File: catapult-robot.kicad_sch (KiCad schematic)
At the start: 15 parts

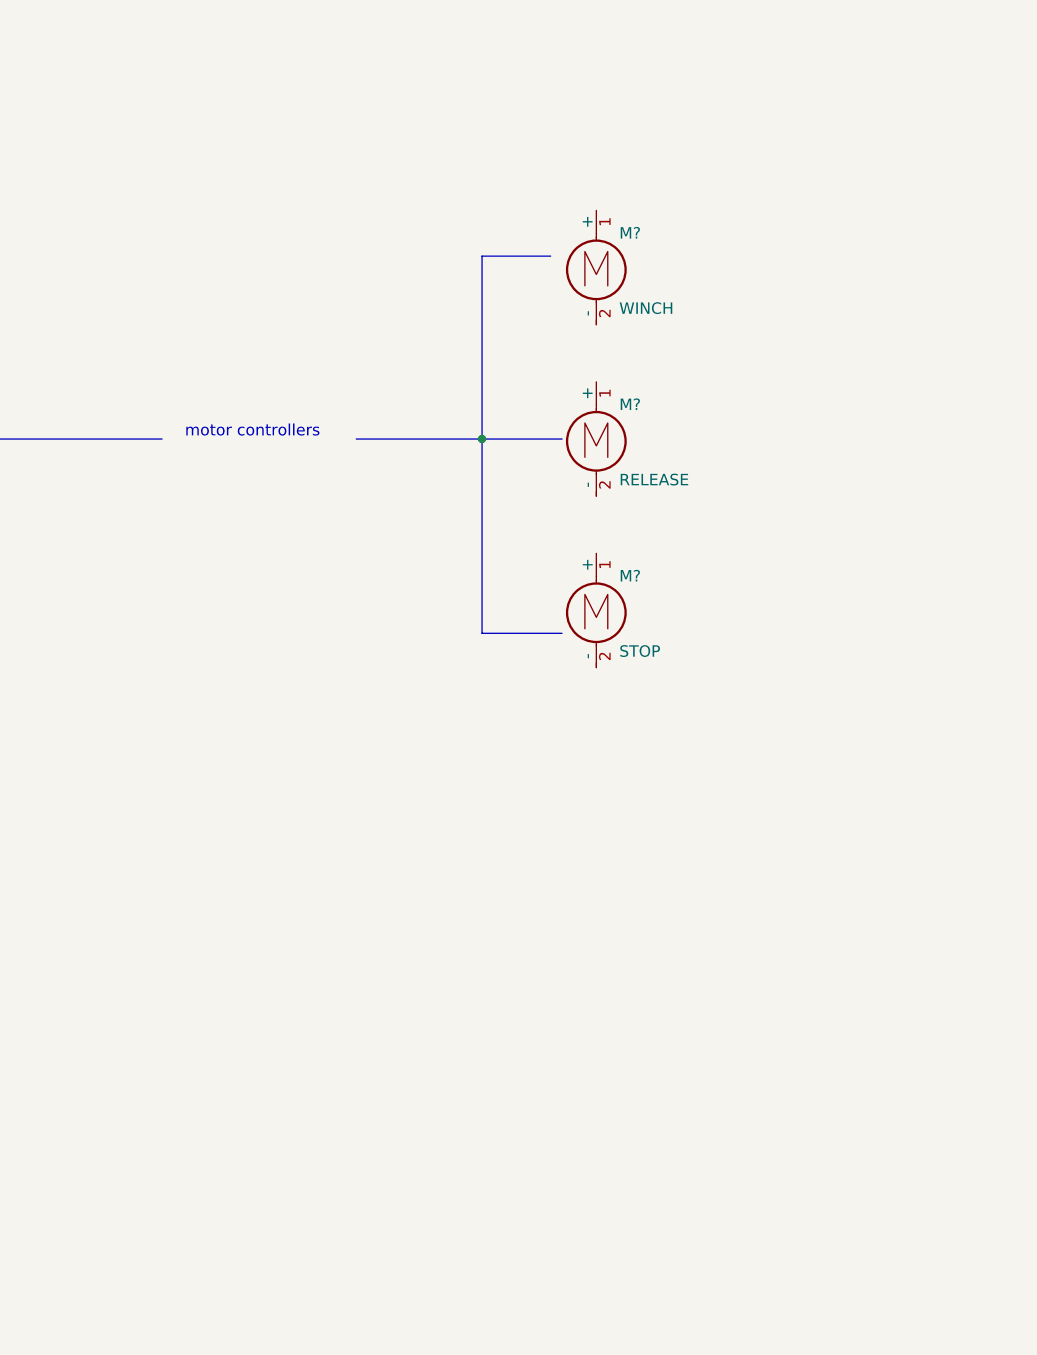
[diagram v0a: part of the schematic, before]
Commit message: Add NCP5901 driver
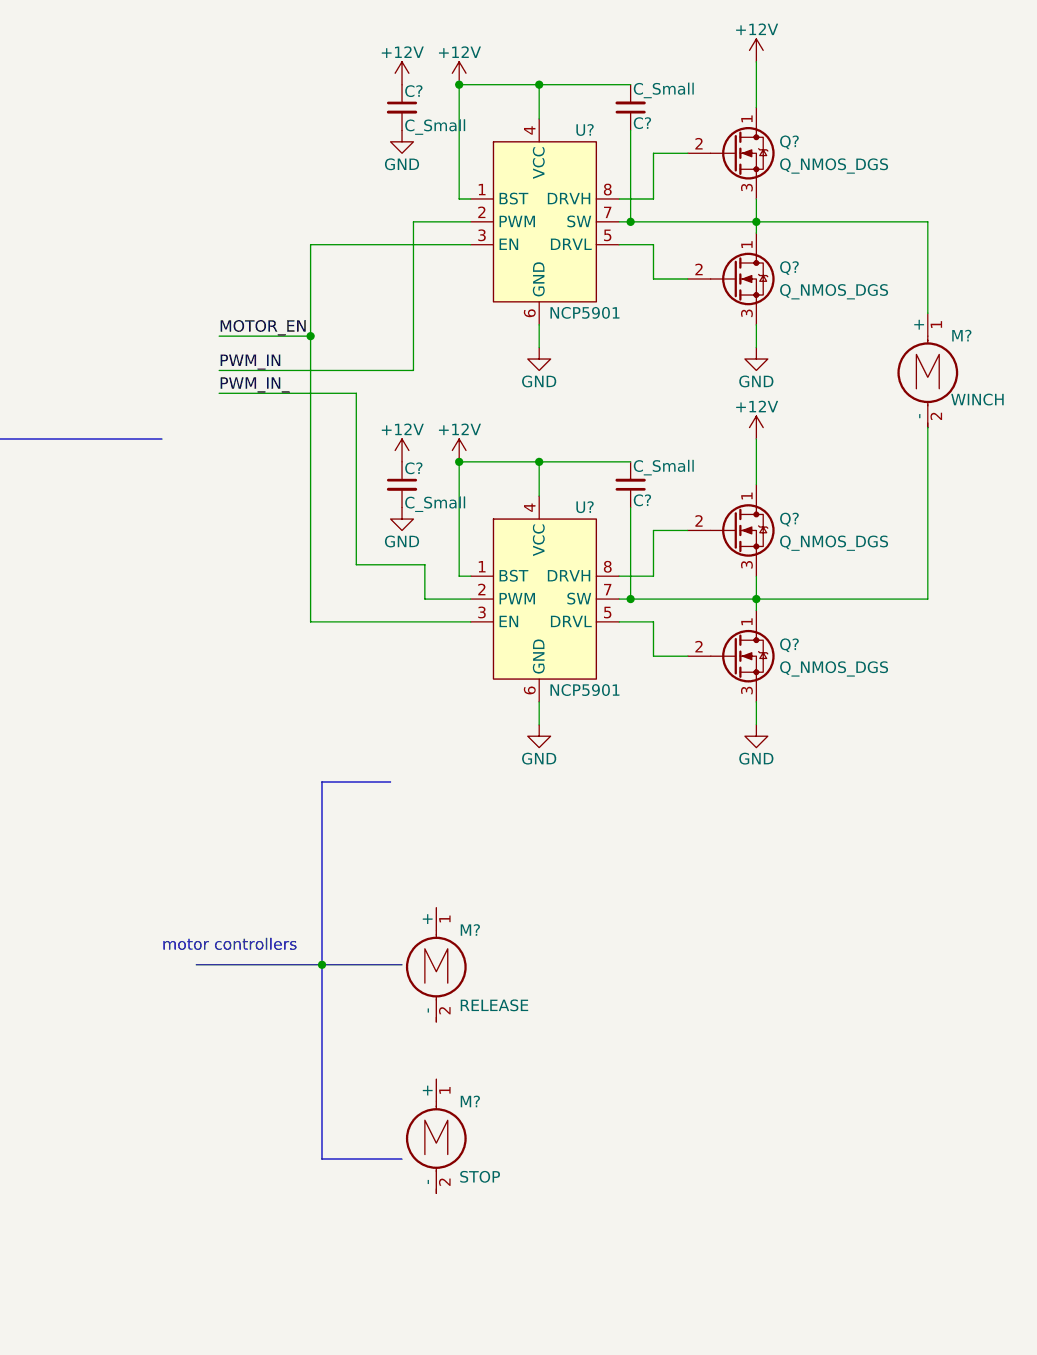
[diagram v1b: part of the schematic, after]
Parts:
- added C? (x4): C_Small, symbol Device:C_Small
- added Q? (x4): Q_NMOS_DGS, symbol Device:Q_NMOS_DGS
- added U? (x2): NCP5901, Package_SO:SOIC-8_3.9x4.9mm_P1.27mm, symbol Catapult:NCP5901
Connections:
- net GND: now also C?.2, C?.2, Q?.3 (S), Q?.3 (S), U?.6 (GND), U?.6 (GND)
- net at M?.1 (+): now also C?.1, Q?.1 (D), Q?.3 (S), U?.7 (SW)
- net at M?.2 (-): now also C?.1, Q?.1 (D), Q?.3 (S), U?.7 (SW)
- new net: Q?.2 (G), U?.5 (DRVL) (x2)
- new net: Q?.2 (G), U?.8 (DRVH) (x2)
- new net +12V: C?.1, C?.1, C?.2, C?.2, Q?.1 (D), Q?.1 (D), U?.1 (BST), U?.1 (BST), U?.4 (VCC), U?.4 (VCC)
- new net MOTOR_EN: U?.3 (EN), U?.3 (EN)
- new net PWM_IN: U?.2 (PWM)
- new net PWM_IN_: U?.2 (PWM)
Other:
- moved on the sheet: M?
